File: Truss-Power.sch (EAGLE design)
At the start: 28 parts, among them J1 XF2L-0535-1, U1 TPS61090, U2 MCP73831T-2ACI/OT, U3 LC709203, U4 LC709203, U5 SC4501, X2 MicroB, X3 22-23-2021

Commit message: Schematics/Board file commit
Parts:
- removed C5: TANT-CAP, NewPart:TANT-CAP
- removed L2: CDRH5D28, NewPart:CDRH5D28
- removed U3: LC709203, NewPart:LC709203
- removed U5: SC4501, NewPart:SC4501
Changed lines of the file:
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@@
 <part name="C3" library="microbuilder" deviceset="CAP_CERAMIC" device="0805-NOOUTLINE" value="10µF"/>
 <part name="U$15" library="microbuilder" deviceset="GND" device=""/>
-<part name="L2" library="NewPart" deviceset="CDRH5D28" device=""/>
-<part name="U3" library="NewPart" deviceset="LC709203" device=""/>
-<part name="U5" library="NewPart" deviceset="SC4501" device=""/>
-<part name="C5" library="NewPart" deviceset="TANT-CAP" device=""/>
 </parts>
 <sheets>
@@
 <instance part="C3" gate="G$1" x="119.38" y="76.2"/>
 <instance part="U$15" gate="G$1" x="119.38" y="68.58"/>
-<instance part="L2" gate="L1" x="40.64" y="-10.16"/>
-<instance part="U3" gate="U1" x="78.74" y="-12.7"/>
-<instance part="U5" gate="U1" x="116.84" y="-12.7"/>
-<instance part="C5" gate="C1" x="35.56" y="-22.86"/>
 </instances>
 <busses>

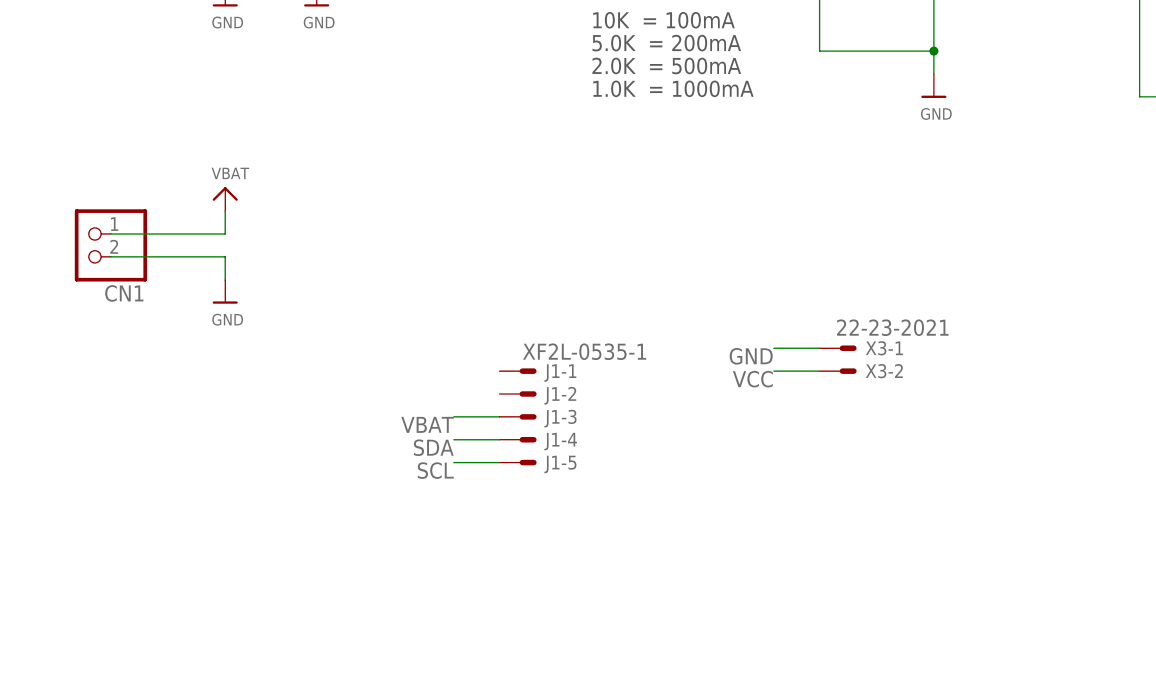
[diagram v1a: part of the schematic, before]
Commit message: Battery Connector Position Change
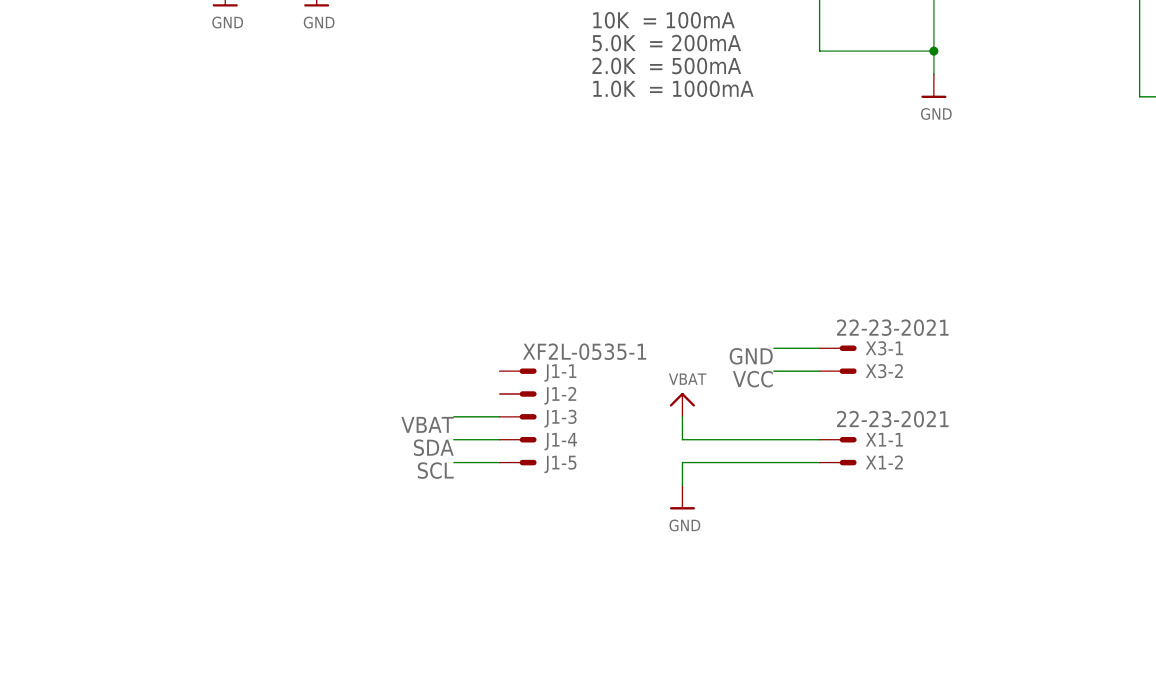
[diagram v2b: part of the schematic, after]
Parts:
- removed CN1: (no value), adafruit:JST_2PIN-SMT-RA
- added X1: 22-23-2021, con-molex:22-23-2021
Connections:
- net GND: now also X1-2.S; no longer CN1.1
- net VBAT: now also X1-1.S; no longer CN1.2
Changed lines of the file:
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@@
 <?xml version="1.0" encoding="utf-8"?>
 <!DOCTYPE eagle SYSTEM "eagle.dtd">
-<eagle version="7.7.0">
+<eagle version="8.3.2">
 <drawing>
 <settings>
 <setting alwaysvectorfont="no"/>
+<setting keepoldvectorfont="yes"/>
 <setting verticaltext="up"/>
 </settings>
@@
 <part name="X2" library="microbuilder" deviceset="USB" device="MICRO_20329" value="MicroB"/>
 <part name="U$18" library="microbuilder" deviceset="VBAT" device=""/>
-<part name="CN1" library="adafruit" deviceset="JST_2PIN" device="-SMT-RA"/>
-<part name="U$1" library="microbuilder" deviceset="VBAT" device=""/>
-<part name="U$4" library="microbuilder" deviceset="GND" device=""/>
 <part name="U4" library="NewPart" deviceset="LC709203" device=""/>
 <part name="P+9" library="supply1" deviceset="VCC" device=""/>
@@
 <part name="C3" library="microbuilder" deviceset="CAP_CERAMIC" device="0805-NOOUTLINE" value="10µF"/>
 <part name="U$15" library="microbuilder" deviceset="GND" device=""/>
+<part name="X1" library="con-molex" library_urn="urn:adsk.eagle:library:165" deviceset="22-23-2021" device=""/>
+<part name="U$16" library="microbuilder" deviceset="VBAT" device=""/>
+<part name="U$17" library="microbuilder" deviceset="GND" device=""/>
 </parts>
 <sheets>
@@
 <instance part="X2" gate="G$1" x="17.78" y="76.2"/>
 <instance part="U$18" gate="G$1" x="129.54" y="88.9"/>
-<instance part="CN1" gate="G$1" x="15.24" y="38.1" rot="R180"/>
-<instance part="U$1" gate="G$1" x="30.48" y="43.18"/>
-<instance part="U$4" gate="G$1" x="30.48" y="30.48"/>
 <instance part="U4" gate="U1" x="172.72" y="63.5"/>
 <instance part="P+9" gate="VCC" x="195.58" y="96.52"/>
@@
 <instance part="C3" gate="G$1" x="119.38" y="76.2"/>
 <instance part="U$15" gate="G$1" x="119.38" y="68.58"/>
+<instance part="X1" gate="-1" x="99.06" y="15.24"/>
+<instance part="X1" gate="-2" x="99.06" y="12.7"/>
+<instance part="U$16" gate="G$1" x="81.28" y="20.32"/>
+<instance part="U$17" gate="G$1" x="81.28" y="7.62"/>
 </instances>
 <busses>
@@
 <wire x1="96.52" y1="58.42" x2="109.22" y2="58.42" width="0.1524" layer="91"/>
 <junction x="109.22" y="58.42"/>
-</segment>
-<segment>
-<pinref part="CN1" gate="G$1" pin="1"/>
-<pinref part="U$4" gate="G$1" pin="GND"/>
-<wire x1="17.78" y1="35.56" x2="30.48" y2="35.56" width="0.1524" layer="91"/>
-<wire x1="30.48" y1="35.56" x2="30.48" y2="33.02" width="0.1524" layer="91"/>
 </segment>
 <segment>
@@
 <wire x1="119.38" y1="73.66" x2="119.38" y2="71.12" width="0.1524" layer="91"/>
 </segment>
+<segment>
+<pinref part="X1" gate="-2" pin="S"/>
+<pinref part="U$17" gate="G$1" pin="GND"/>
+<wire x1="96.52" y1="12.7" x2="81.28" y2="12.7" width="0.1524" layer="91"/>
+<wire x1="81.28" y1="12.7" x2="81.28" y2="10.16" width="0.1524" layer="91"/>
+</segment>
 </net>
 <net name="N$12" class="0">
@@
 <pinref part="C3" gate="G$1" pin="1"/>
 <junction x="119.38" y="81.28"/>
-</segment>
-<segment>
-<pinref part="CN1" gate="G$1" pin="2"/>
-<pinref part="U$1" gate="G$1" pin="VBAT"/>
-<wire x1="17.78" y1="38.1" x2="30.48" y2="38.1" width="0.1524" layer="91"/>
-<wire x1="30.48" y1="38.1" x2="30.48" y2="40.64" width="0.1524" layer="91"/>
 </segment>
 <segment>
@@
 <wire x1="60.96" y1="17.78" x2="55.88" y2="17.78" width="0.1524" layer="91"/>
 <label x="55.88" y="17.78" size="1.778" layer="95" rot="R180"/>
+</segment>
+<segment>
+<pinref part="U$16" gate="G$1" pin="VBAT"/>
+<pinref part="X1" gate="-1" pin="S"/>
+<wire x1="81.28" y1="17.78" x2="81.28" y2="15.24" width="0.1524" layer="91"/>
+<wire x1="81.28" y1="15.24" x2="96.52" y2="15.24" width="0.1524" layer="91"/>
 </segment>
 </net>
@@
 </schematic>
 </drawing>
+<compatibility>
+<note version="8.2" severity="warning">
+Since Version 8.2, EAGLE supports online libraries. The ids
+of those online libraries will not be understood (or retained)
+with this version.
+</note>
+</compatibility>
 </eagle>

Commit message: TrussPower V2
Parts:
- removed U4: LC709203, NewPart:LC709203
- added C5: 1uF, rcl:C-EUC0603
- added LED1: (no value), led:LEDCHIP-LED0603
- added R11: 180, resistor:R-US_R0402
- added R12: 4.7K, resistor:R-US_R0402
- added R13: 330, resistor:R-US_R0402
- added R6: 1K, resistor:R-US_R0402
- added U3: MAX17044, NewPart:MAX17044
- C11: value 1uF -> 10nF
- R10, R8: value 10K -> 4.7K
- R7: device microbuilder:RESISTOR0805_NOOUTLINE -> resistor:R-US_R0402
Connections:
- new net ALRT: J1-2.MS, R12.2, U3./ALRT
- new net LEDSOC: J1-1.MSV, LED1.A
- new net N$1: C5.1, R6.2, U3.CELL
- new net N$3: C11.1, R11.2, U3.VDD
- new net N$4: LED1.C, R13.2
- net GND: now also C5.2, R13.1, U3.CTG, U3.EPAD, U3.GND, U3.QSTRT; no longer U4.ALARMB, U4.EPAD, U4.TEST, U4.VSS
- net N$12: now also R7.2; no longer R7.1
- net N$13: now also R7.1; no longer R7.2
- net SCL: now also R10.1, U3.SCL; no longer R8.1, U4.SCL
- net SDA: now also R8.1, U3.SDA; no longer R10.1, U4.SDA
- net VBAT: now also R11.1, R6.1; no longer C11.1, U4.VDD
- net VCC: now also R12.1
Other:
- moved on the sheet: C11
